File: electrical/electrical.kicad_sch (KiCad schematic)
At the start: 0 parts

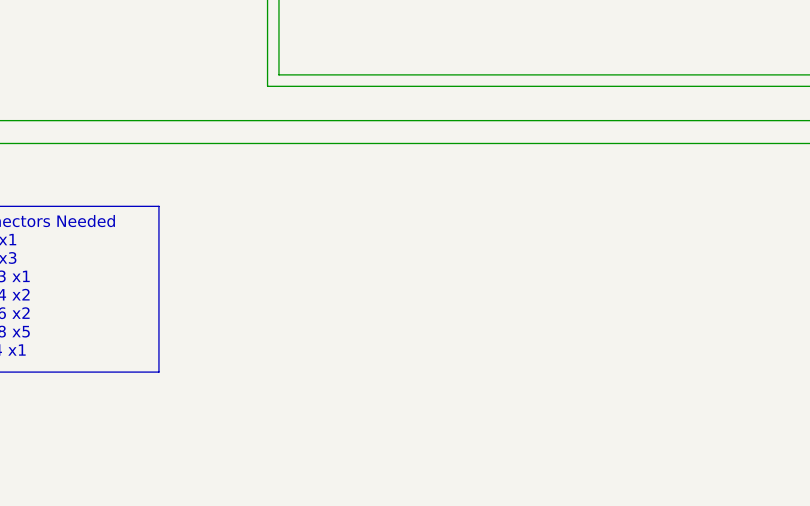
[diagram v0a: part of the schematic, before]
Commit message: Added RS232 and Canbus wiring notation
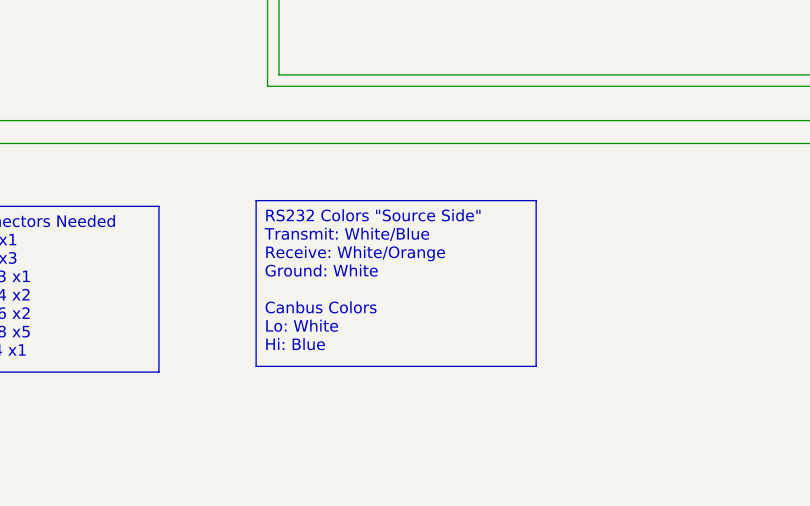
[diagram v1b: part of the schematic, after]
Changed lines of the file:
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@@
 	(title_block
 		(title "Electrical Overview")
-		(date "2025-10-01")
-		(rev "1.1.1")
+		(date "2025-10-02")
+		(rev "1.1.4")
 		(company "N78HR")
 	)
@@
 		(margins 0.9525 0.9525 0.9525 0.9525)
 		(stroke
+			(width 0)
+			(type solid)
+		)
+		(fill
+			(type none)
+		)
+		(effects
+			(font
+				(size 1.27 1.27)
+			)
+			(justify left top)
+		)
+	)
+	(text_box "RS232 Colors \"Source Side\"\nTransmit: White/Blue\nReceive: White/Orange\nGround: White\n\nCanbus Colors\nLo: White\nHi: Blue"
+		(exclude_from_sim no)
+		(at 109.22 233.68 0)
+		(size 31.115 18.415)
+		(margins 0.9525 0.9525 0.9525 0.9525)
+		(stroke

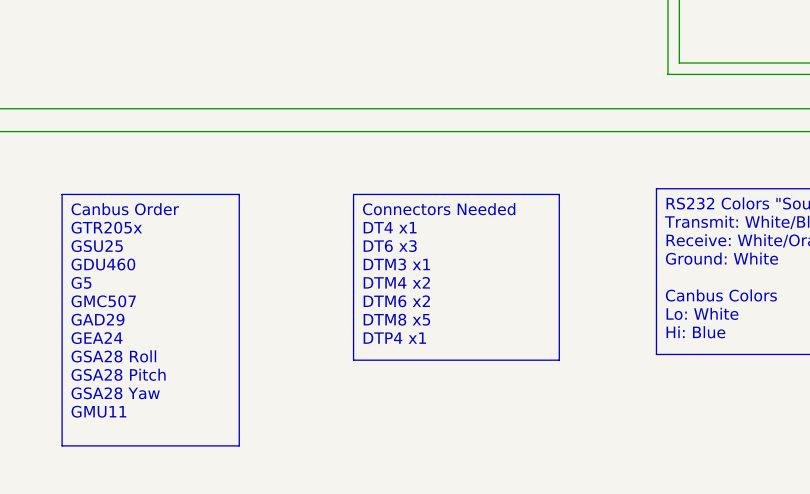
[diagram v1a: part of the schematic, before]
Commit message: Added connector for GTP 59.
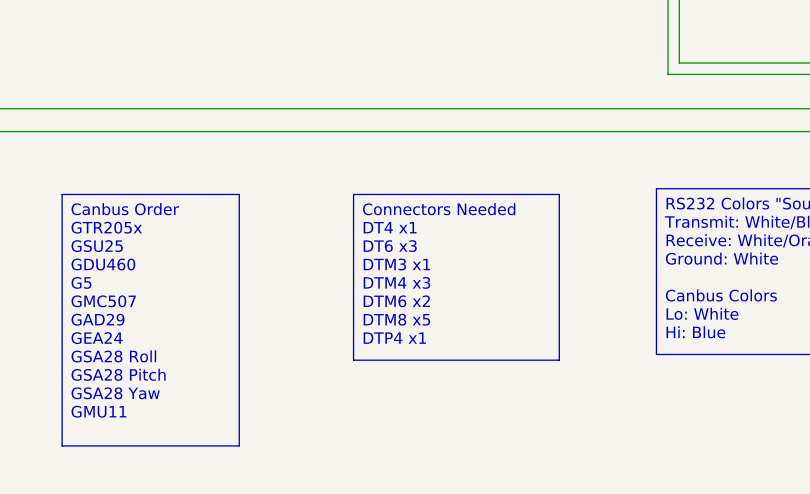
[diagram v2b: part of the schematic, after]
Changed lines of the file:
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@@
 	(title_block
 		(title "Electrical Overview")
-		(date "2025-10-02")
-		(rev "1.1.4")
+		(date "2025-10-03")
+		(rev "1.1.5")
 		(company "N78HR")
 	)
@@
 		)
 	)
-	(text_box "Connectors Needed\nDT4 x1\nDT6 x3\nDTM3 x1\nDTM4 x2\nDTM6 x2\nDTM8 x5\nDTP4 x1"
+	(text_box "Connectors Needed\nDT4 x1\nDT6 x3\nDTM3 x1\nDTM4 x3\nDTM6 x2\nDTM8 x5\nDTP4 x1"
 		(exclude_from_sim no)
 		(at 75.565 234.315 0)

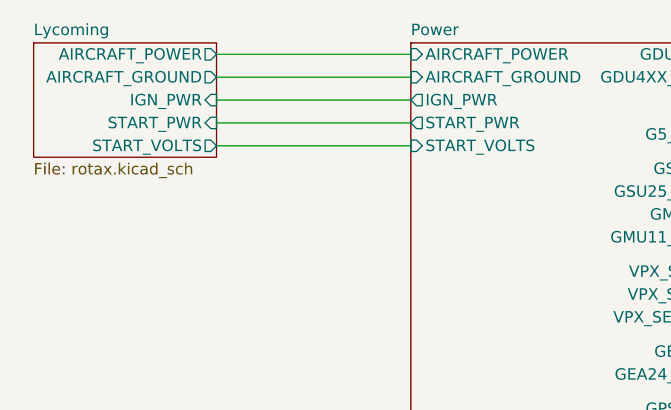
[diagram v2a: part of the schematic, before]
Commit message: Added Field Wire and Alternator symbol.
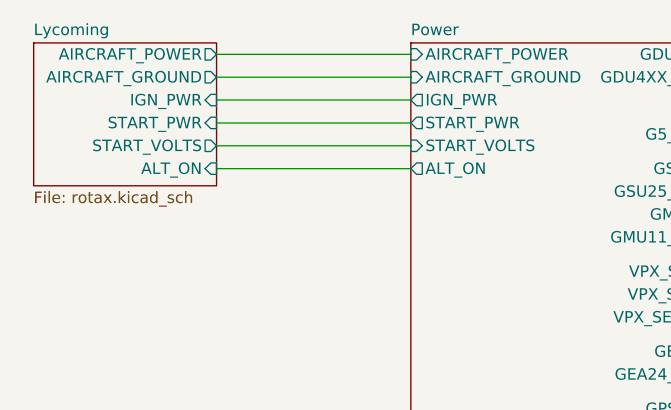
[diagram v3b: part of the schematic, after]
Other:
- sheet Lycoming ports: added ALT_ON; removed none
- sheet Power ports: added ALT_ON; removed none
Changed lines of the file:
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@@
 	(title_block
 		(title "Electrical Overview")
-		(date "2025-10-03")
-		(rev "1.1.5")
+		(date "2025-10-15")
+		(rev "1.1.14")
 		(company "N78HR")
 	)
@@
 		(pts
 			(xy 185.42 179.07) (xy 189.23 179.07)
+		)
+		(stroke
+			(width 0)
+			(type default)
+		)
+	)
+	(wire
+		(pts
+			(xy 36.83 43.18) (xy 58.42 43.18)
 		)
 		(stroke
@@
 			)
 		)
+		(pin "ALT_ON" output
+			(at 58.42 43.18 180)
+			(effects
+				(font
+					(size 1.27 1.27)
+				)
+				(justify left)
+			)
+		)
 		(instances
 			(project "electrical"
@@
 	(sheet
 		(at 16.51 29.21)
-		(size 20.32 12.7)
+		(size 20.32 15.875)
 		(exclude_from_sim no)
 		(in_bom yes)
@@
 		)
 		(property "Sheetfile" "rotax.kicad_sch"
-			(at 16.51 42.4946 0)
+			(at 16.51 45.6696 0)
 			(effects
 				(font
@@
 			(effects
 				(font
+					(size 1.27 1.27)
+				)
+				(justify right)
+			)
+		)
+		(pin "ALT_ON" input
+			(at 36.83 43.18 0)
+			(effects
+				(font

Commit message: Added lighting bus
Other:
- sheet Autopilot ports: added LIGHTS_HI; removed none
- sheet Communication ports: added LIGHTS_HI; removed none
- sheet Navigator ports: added LIGHTS_HI; removed none
- sheet PFD ports: added LIGHTS_HI; removed none
- sheet Power ports: added LIGHTS_HI; removed none
- sheet Transponder ports: added LIGHTS_HI; removed none
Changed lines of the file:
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@@
 	(title_block
 		(title "Electrical Overview")
-		(date "2025-10-15")
-		(rev "1.1.14")
+		(date "2025-10-19")
+		(rev "1.1.15")
 		(company "N78HR")
 	)
@@
 	(wire
 		(pts
+			(xy 346.71 181.61) (xy 351.79 181.61)
+		)
+		(stroke
+			(width 0)
+			(type default)
+		)
+	)
+	(wire
+		(pts
 			(xy 351.79 227.33) (xy 351.79 190.5)
 		)
@@
 	(wire
 		(pts
+			(xy 168.91 97.79) (xy 173.99 97.79)
+		)
+		(stroke
+			(width 0)
+			(type default)
+		)
+	)
+	(wire
+		(pts
 			(xy 220.98 99.06) (xy 284.48 99.06)
 		)
@@
 	(wire
 		(pts
+			(xy 227.33 204.47) (xy 232.41 204.47)
+		)
+		(stroke
+			(width 0)
+			(type default)
+		)
+	)
+	(wire
+		(pts
 			(xy 220.98 107.95) (xy 257.81 107.95)
 		)
@@
 	(wire
 		(pts
+			(xy 97.79 123.19) (xy 102.87 123.19)
+		)
+		(stroke
+			(width 0)
+			(type default)
+		)
+	)
+	(wire
+		(pts
 			(xy 303.53 53.34) (xy 303.53 68.58)
 		)
@@
 	(wire
 		(pts
+			(xy 356.87 85.09) (xy 365.76 85.09)
+		)
+		(stroke
+			(width 0)
+			(type default)
+		)
+	)
+	(wire
+		(pts
 			(xy 97.79 57.15) (xy 173.99 57.15)
 		)
@@
 	(wire
 		(pts
+			(xy 356.87 38.1) (xy 365.76 38.1)
+		)
+		(stroke
+			(width 0)
+			(type default)
+		)
+	)
+	(wire
+		(pts
 			(xy 36.83 35.56) (xy 58.42 35.56)
 		)
@@
 		)
 	)
+	(global_label "LIGHTS_HI"
+		(shape input)
+		(at 232.41 204.47 0)
+		(fields_autoplaced yes)
+		(effects
+			(font
+				(size 1.27 1.27)
+			)
+			(justify left)
+		)
+		(property "Intersheetrefs" "${INTERSHEET_REFS}"
+			(at 244.7086 204.47 0)
+			(effects
+				(font
+					(size 1.27 1.27)
+				)
+				(justify left)
+				(hide yes)
+			)
+		)
+	)
 	(global_label "GAD29_PWR"
 		(shape input)
@@
 		)
 	)
+	(global_label "LIGHTS_HI"
+		(shape input)
+		(at 365.76 85.09 0)
+		(fields_autoplaced yes)
+		(effects
+			(font
+				(size 1.27 1.27)
+			)
+			(justify left)
+		)
+		(property "Intersheetrefs" "${INTERSHEET_REFS}"
+			(at 378.0586 85.09 0)
+			(effects
+				(font
+					(size 1.27 1.27)
+				)
+				(justify left)
+				(hide yes)
+			)
+		)
+	)
+	(global_label "LIGHTS_HI"
+		(shape input)
+		(at 168.91 97.79 180)
+		(fields_autoplaced yes)
+		(effects
+			(font
+				(size 1.27 1.27)
+			)
+			(justify right)
+		)
+		(property "Intersheetrefs" "${INTERSHEET_REFS}"
+			(at 156.6114 97.79 0)
+			(effects
+				(font
+					(size 1.27 1.27)
+				)
+				(justify right)
+				(hide yes)
+			)
+		)
+	)
+	(global_label "LIGHTS_HI"
+		(shape input)
+		(at 365.76 38.1 0)
+		(fields_autoplaced yes)
+		(effects
+			(font
+				(size 1.27 1.27)
+			)
+			(justify left)
+		)
+		(property "Intersheetrefs" "${INTERSHEET_REFS}"
+			(at 378.0586 38.1 0)
+			(effects
+				(font
+					(size 1.27 1.27)
+				)
+				(justify left)
+				(hide yes)
+			)
+		)
+	)
 	(global_label "GPS175_BAK_PWR"
 		(shape input)
@@
 		)
 	)
+	(global_label "LIGHTS_HI"
+		(shape output)
+		(at 102.87 123.19 0)
+		(fields_autoplaced yes)
+		(effects
+			(font
+				(size 1.27 1.27)
+			)
+			(justify left)
+		)
+		(property "Intersheetrefs" "${INTERSHEET_REFS}"
+			(at 115.1686 123.19 0)
+			(effects
+				(font
+					(size 1.27 1.27)
+				)
+				(justify left)
+				(hide yes)
+			)
+		)
+	)
 	(global_label "GSA28_PWR"
 		(shape output)
@@
 		)
 	)
+	(global_label "LIGHTS_HI"
+		(shape input)
+		(at 351.79 181.61 0)
+		(fields_autoplaced yes)
+		(effects
+			(font
+				(size 1.27 1.27)
+			)
+			(justify left)
+		)
+		(property "Intersheetrefs" "${INTERSHEET_REFS}"
+			(at 364.0886 181.61 0)
+			(effects
+				(font
+					(size 1.27 1.27)
+				)
+				(justify left)
+				(hide yes)
+			)
+		)
+	)
 	(global_label "GPS175_PWR"
 		(shape output)
@@
 			)
 		)
+		(pin "LIGHTS_HI" output
+			(at 97.79 123.19 0)
+			(effects
+				(font
+					(size 1.27 1.27)
+				)
+				(justify right)
+			)
+		)
 		(instances
 			(project "electrical"
@@
 			)
 		)
+		(pin "LIGHTS_HI" input
+			(at 356.87 38.1 0)
+			(effects
+				(font
+					(size 1.27 1.27)
+				)
+				(justify right)
+			)
+		)
 		(instances
 			(project "electrical"
@@
 			)
 		)
+		(pin "LIGHTS_HI" input
+			(at 173.99 97.79 180)
+			(effects
+				(font
+					(size 1.27 1.27)
+				)
+				(justify left)
+			)
+		)
 		(instances
 			(project "electrical"
@@
 			)
 		)
+		(pin "LIGHTS_HI" input
+			(at 356.87 85.09 0)
+			(effects
+				(font
+					(size 1.27 1.27)
+				)
+				(justify right)
+			)
+		)
 		(instances
 			(project "electrical"
@@
 			)
 		)
+		(pin "LIGHTS_HI" input
+			(at 227.33 204.47 0)
+			(effects
+				(font
+					(size 1.27 1.27)
+				)
+				(justify right)
+			)
+		)
 		(instances
 			(project "electrical"
@@
 			(effects
 				(font
+					(size 1.27 1.27)
+				)
+				(justify right)
+			)
+		)
+		(pin "LIGHTS_HI" input
+			(at 346.71 181.61 0)
+			(effects
+				(font
